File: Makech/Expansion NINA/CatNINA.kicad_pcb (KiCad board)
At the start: 2 copper layers, 22.9 x 30.9 mm, 10 parts, among them J1 ESP, U1 ESP32-WROOM

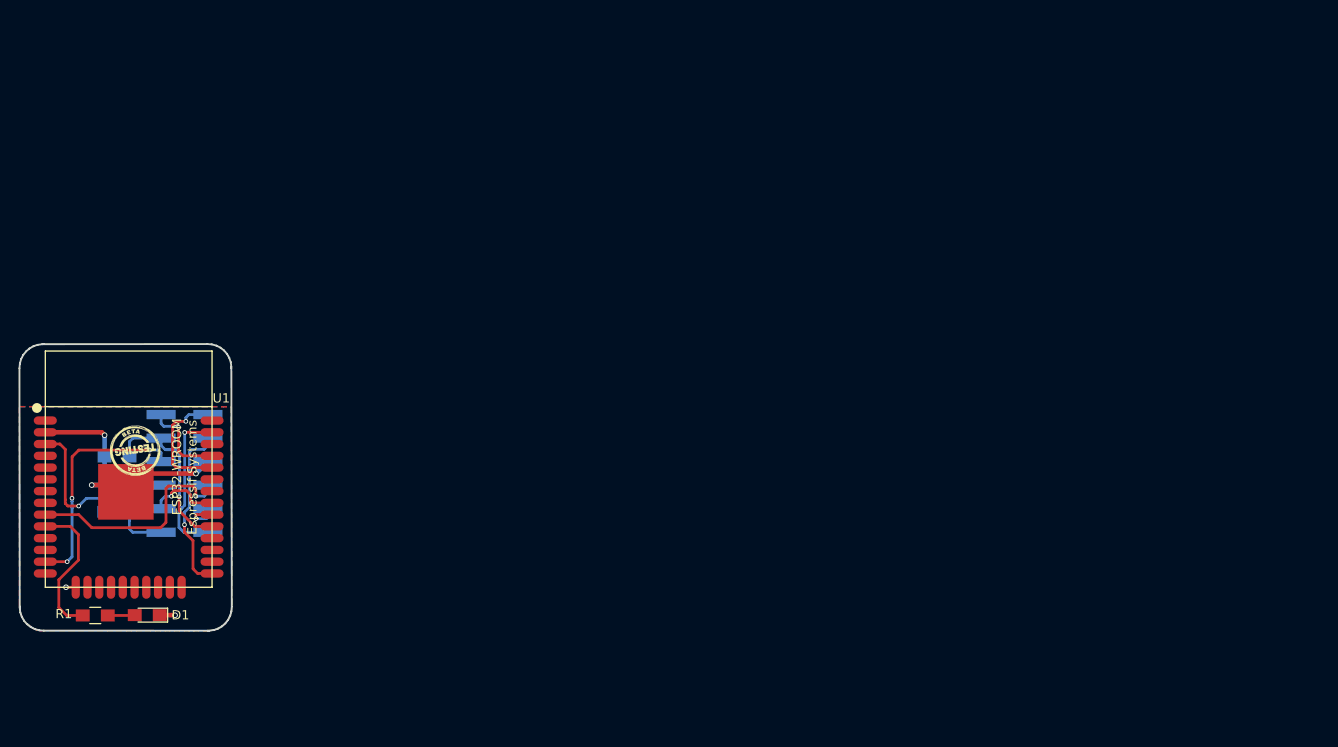
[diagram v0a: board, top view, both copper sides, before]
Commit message: move connector
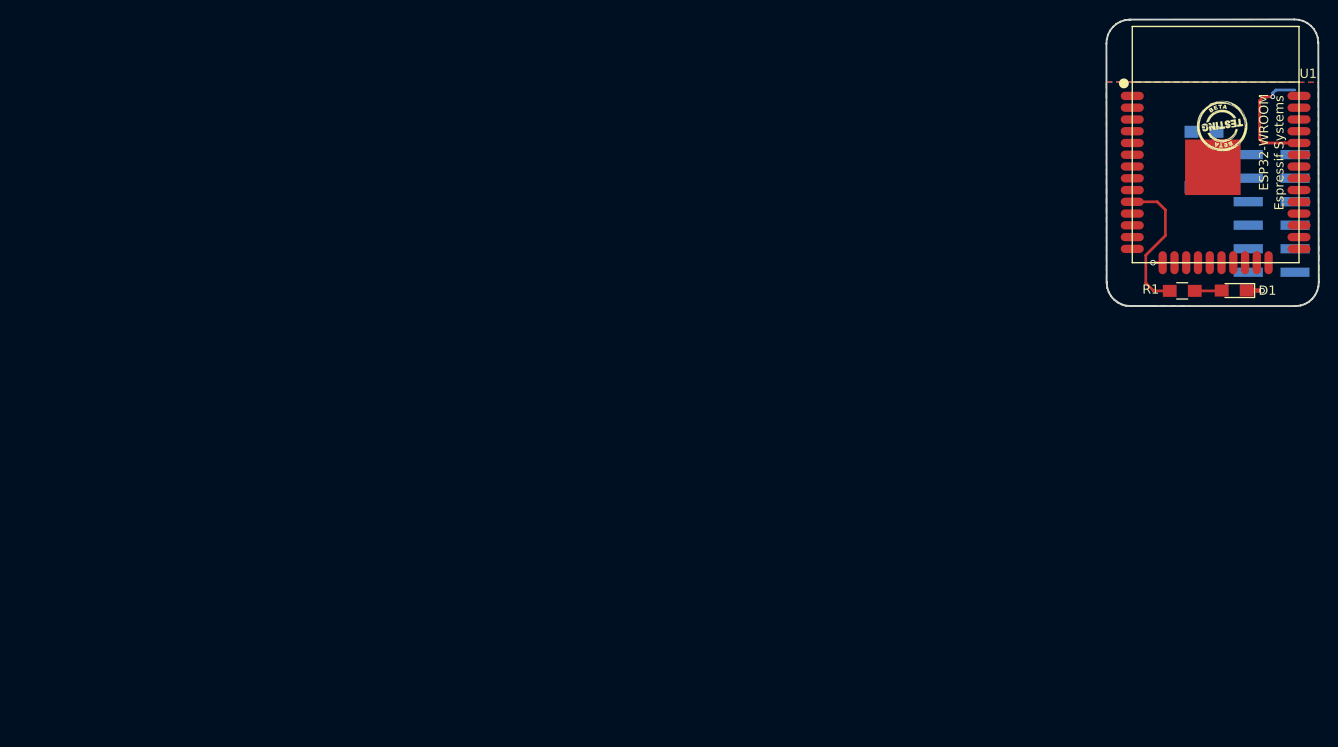
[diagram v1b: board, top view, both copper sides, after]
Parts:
- moved R2 122.5 mm to (243.8, 61.7)
- moved R3 122.5 mm to (243.9, 55.7)
- moved C1 122.5 mm to (244.0, 58.8)
- moved D1 122.5 mm to (247.1, 72.8)
- moved G*** 122.5 mm to (237.8, 70.5)
- moved G*** 122.5 mm to (251.3, 71.0)
- moved G*** 122.5 mm to (245.8, 55.0)
- moved R1 122.5 mm to (241.5, 72.9)
- moved U1 122.5 mm to (245.1, 57.1)
- moved J1 120.7 mm to (251.2, 64.5)
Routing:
- net /ESP_MOSI: track 25.2 -> 0.00 mm, vias 3 -> 0
- net /ESP_BUSY: track 24.6 -> 0.00 mm, vias 1 -> 0
- net /ESP_RESET: track 22.3 -> 0.00 mm, vias 1 -> 0
- net /ESP_CS: track 19.6 -> 0.00 mm, vias 1 -> 0
- net /ESP_GPIO0: track 18.5 -> 0.00 mm, vias 1 -> 0
- net +3V3: track 17.6 -> 0.00 mm, vias 1 -> 0
- net /ESP_MISO: track 17.2 -> 0.00 mm, vias 1 -> 0
- net GND: track 18.5 -> 2.71 mm, vias 4 -> 2
- net /ESP_TX: track 9.44 -> 0.00 mm, vias 1 -> 0
- net /ESP_RTS: track 7.96 -> 0.00 mm, vias 1 -> 0
- net /ESP_SCK: track 4.39 -> 0.00 mm, vias 1 -> 0

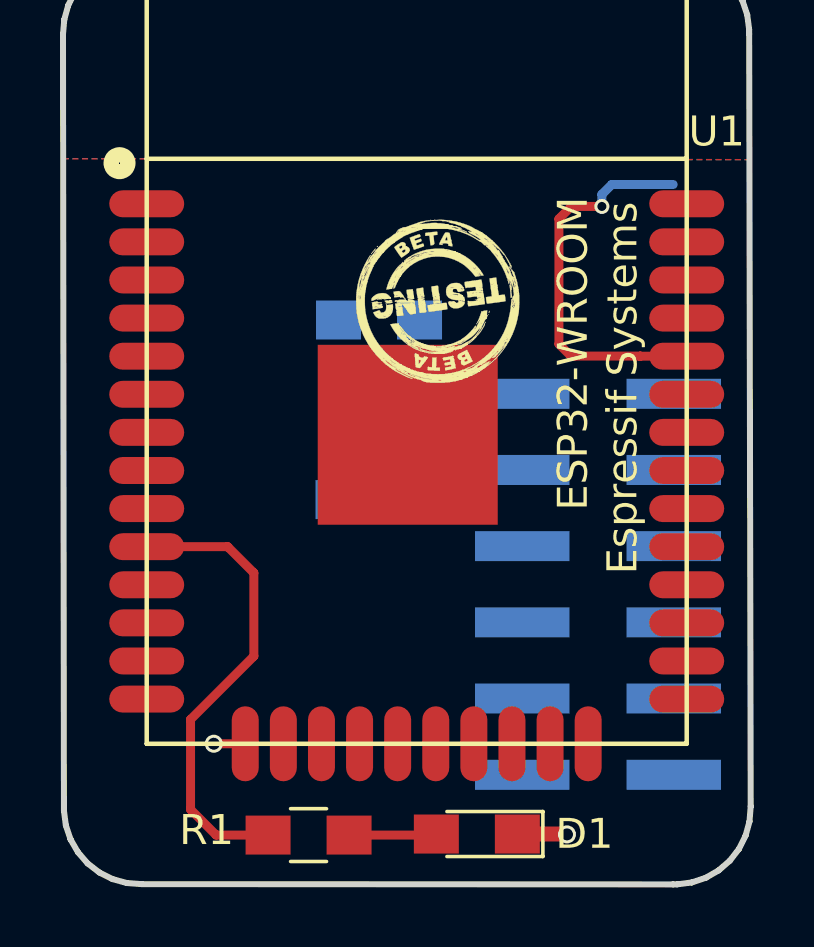
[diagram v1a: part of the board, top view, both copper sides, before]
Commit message: routeo moved connector
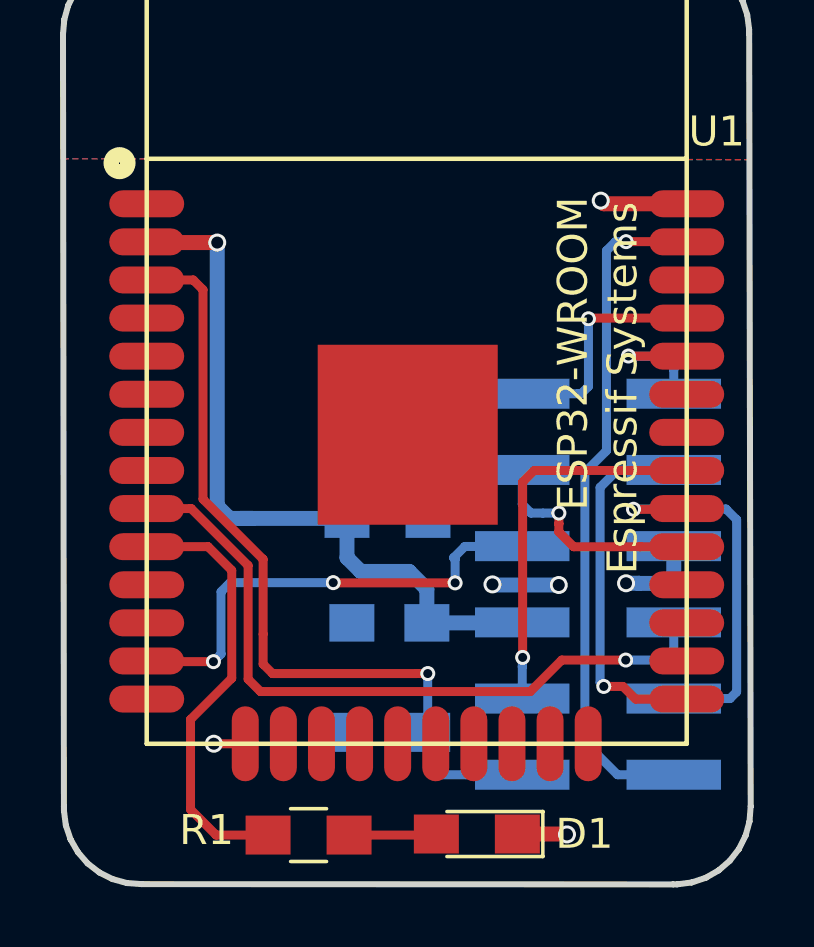
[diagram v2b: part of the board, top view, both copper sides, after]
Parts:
- G***: moved to B.Cu
- moved G*** 18.9 mm to (238.0, 57.7)
- moved R2 7.77 mm to (244.1, 69.4)
- moved C1 7.01 mm to (244.2, 65.8)
- moved R3 6.62 mm to (244.1, 62.3)
- moved G*** 1.58 mm to (244.7, 56.0)
- moved G*** 0.61 mm to (237.8, 69.9)
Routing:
- net /ESP_RESET: track 0.00 -> 27.2 mm, vias 0 -> 1
- net +3V3: track 0.00 -> 24.8 mm, vias 0 -> 1
- net /ESP_BUSY: track 0.00 -> 23.8 mm, vias 0 -> 1
- net /ESP_MISO: track 0.00 -> 22.9 mm, vias 0 -> 1
- net /ESP_MOSI: track 0.00 -> 16.0 mm, vias 0 -> 3
- net /ESP_SCK: track 0.00 -> 13.3 mm, vias 0 -> 1
- net /ESP_RTS: track 0.00 -> 12.9 mm, vias 0 -> 1
- net /ESP_GPIO0: track 0.00 -> 12.4 mm, vias 0 -> 1
- net /ESP_CS: track 0.00 -> 12.0 mm, vias 0 -> 1
- net /ESP_RX: track 13.1 -> 4.60 mm
- net GND: track 2.71 -> 10.9 mm, vias 2 -> 6
- net /ESP_TX: track 0.00 -> 7.88 mm, vias 0 -> 1
- net /IO25: track 15.6 -> 14.6 mm

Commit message: mesures
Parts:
- moved C1 95.6 mm to (160.2, 111.3)
- moved G*** 95.6 mm to (160.7, 101.5)
- moved D1 95.6 mm to (163.1, 118.3)
- moved G*** 95.6 mm to (153.8, 115.4)
- moved G*** 95.6 mm to (153.9, 103.2)
- moved R1 95.6 mm to (157.5, 118.4)
- moved R3 95.6 mm to (160.1, 107.8)
- moved J1 95.6 mm to (167.1, 110.0)
- moved R2 95.6 mm to (160.1, 115.0)
- moved U1 95.6 mm to (161.1, 102.6)
